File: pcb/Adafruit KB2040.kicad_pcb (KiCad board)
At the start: 2 copper layers, 107.2 x 23.5 mm, 12 parts, among them M1 Vibrating-Motor, SW1 SW_SPST, U1 kb2040, U2 2465

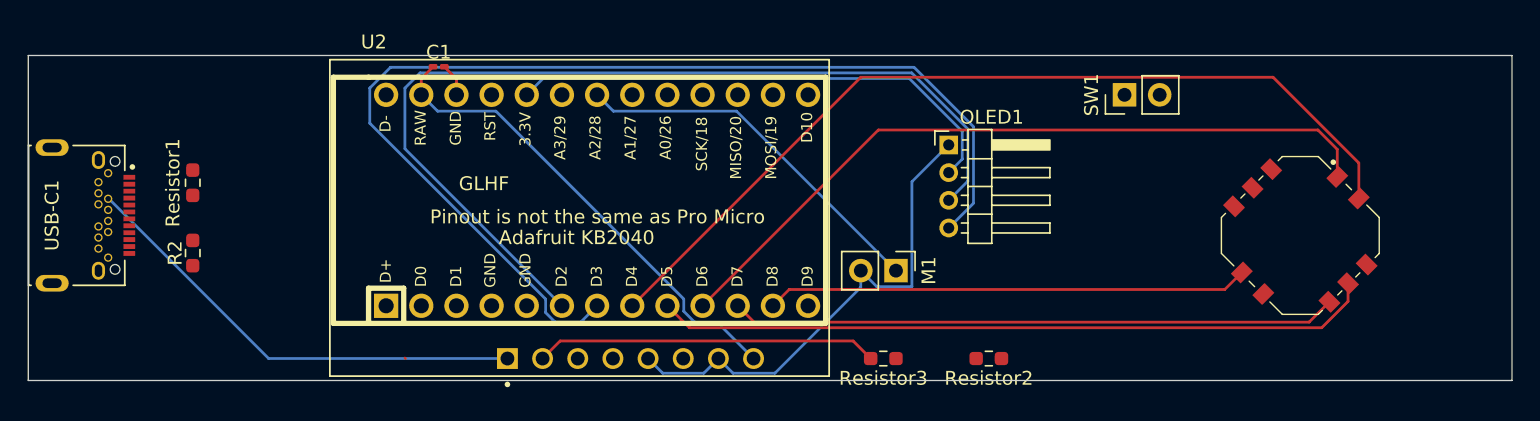
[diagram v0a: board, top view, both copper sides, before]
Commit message: gotta redo the board brahhh - the oled cant fit in the current orientation.
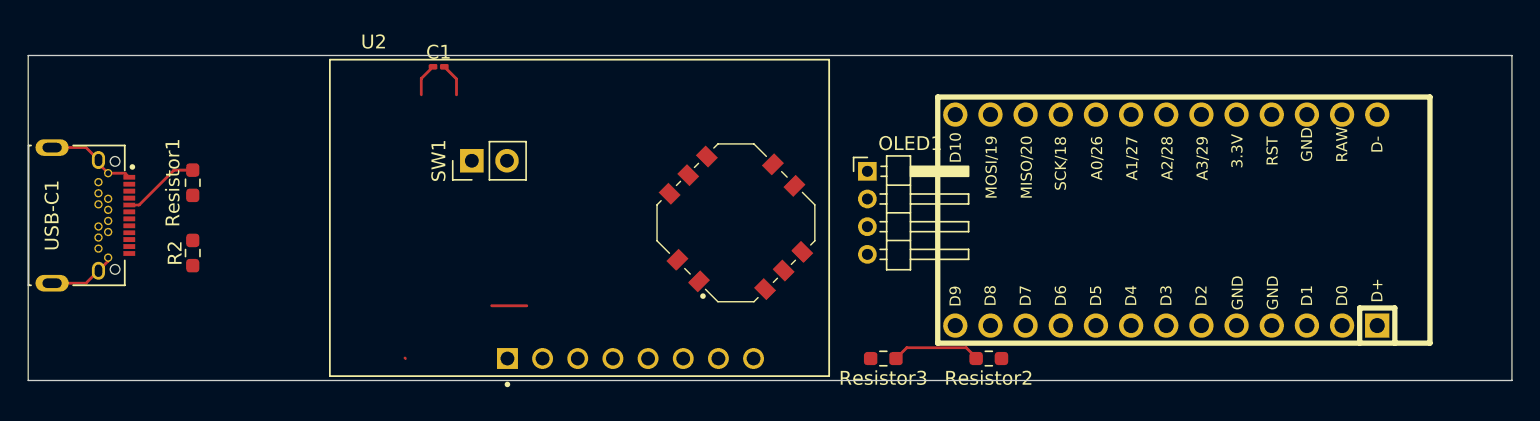
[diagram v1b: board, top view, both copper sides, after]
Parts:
- removed M1: Vibrating-Motor, Connector_PinHeader_2.54mm:PinHeader_1x02_P2.54mm_Vertical
- U1: moved to B.Cu
- moved SW1 47.4 mm to (116.7, 61.9)
- moved U1 43.7 mm to (168.1, 66.2)
- moved D-Pad1 40.8 mm to (135.8, 66.4), turned to 180 degrees
- moved OLED1 6.17 mm to (145.3, 62.7)
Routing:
- net SDA: track 80.0 -> 0.00 mm
- net SDL: track 68.9 -> 0.00 mm
- net D8ASSY: track 64.5 -> 0.00 mm
- net D10ASSY: track 53.7 -> 0.00 mm
- net Net-(U1-D5): track 51.9 -> 0.00 mm
- net Net-(U1-D7): track 43.8 -> 0.00 mm
- net +3.3V: track 36.9 -> 0.00 mm
- net Net-(U1-D8): track 34.9 -> 0.00 mm
- net VBUS: track 33.6 -> 0.00 mm
- net +5V: track 34.8 -> 2.43 mm
- net Net-(M1-+): track 26.9 -> 0.00 mm
- net Net-(U2-VLIPO): track 24.8 -> 0.00 mm
- net GND: track 38.3 -> 16.5 mm
- net Net-(U1-A0/26): track 0.00 -> 6.48 mm
- net Net-(USB-C1-CC1): track 0.00 -> 5.63 mm

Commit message: I messed around with the wiring more - now it should be done. need to do some final checks before sent off (whatever that means)
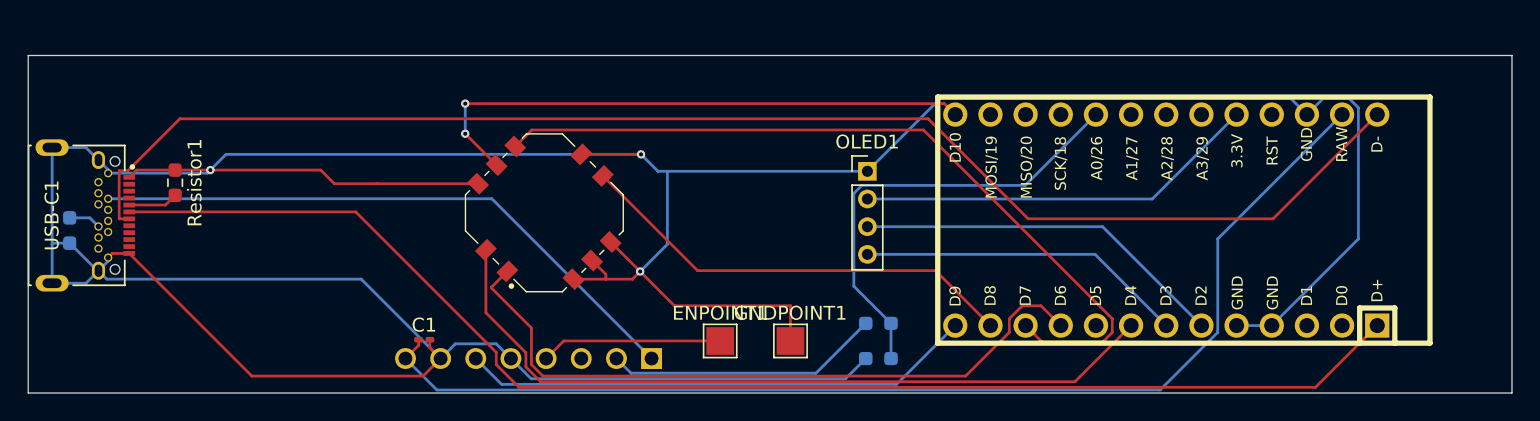
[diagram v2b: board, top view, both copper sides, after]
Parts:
- removed SW1: SW_SPST, Connector_PinHeader_2.54mm:PinHeader_1x02_P2.54mm_Vertical
- added ENPOINT1: TestPoint_Small, TestPoint:TestPoint_Pad_2.0x2.0mm, F.Cu at (134.6, 74.9)
- added GNDPOINT1: TestPoint_Small, TestPoint:TestPoint_Pad_2.0x2.0mm, F.Cu at (139.7, 74.9)
- OLED1: footprint Connector_PinHeader_2.00mm:PinHeader_1x04_P2.00mm_Horizontal -> Connector_PinHeader_2.00mm:PinHeader_1x04_P2.00mm_Vertical
- R2, Resistor2, Resistor3, U2: moved to B.Cu
- moved C1 19.7 mm to (113.2, 74.8)
- moved D-Pad1 13.9 mm to (121.9, 65.7)
- moved R2 9.04 mm to (87.6, 67.0), turned to 90 degrees
- moved Resistor2 7.98 mm to (146.1, 76.2), turned to 0 degrees
- moved Resistor3 2.57 mm to (146.1, 73.7)
- moved Resistor1 1.27 mm to (95.2, 63.5), turned to -90 degrees
- turned U2 to 180 degrees
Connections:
- D-Pad1 pad 1: D10ASSY -> D6ASSY
- D-Pad1 pad 4: Net-(U1-D5) -> D10ASSY
- U1 pad 10: D10ASSY -> D6ASSY
- U1 pad 20: Net-(M1-+) -> unconnected-(U1-A2/28-Pad20)
- U1 pad 26: unconnected-(U1-D10-Pad26) -> D10ASSY
- U1 pad 9: Net-(U1-D5) -> unconnected-(U1-D5-Pad9)
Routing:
- net GND: track 16.5 -> 292.2 mm, vias 0 -> 3
- net D-: track 0.00 -> 102.7 mm
- net D+: track 0.00 -> 97.8 mm
- net +5V: track 2.43 -> 82.5 mm
- net Net-(U1-D7): track 0.00 -> 57.3 mm
- net D8ASSY: track 0.00 -> 55.5 mm
- net D6ASSY: track 0.00 -> 50.3 mm
- net VBUS: track 0.00 -> 44.0 mm
- net D10ASSY: track 0.00 -> 41.1 mm, vias 0 -> 2
- net LBO: track 0.00 -> 37.2 mm
- net Net-(U1-D8): track 0.00 -> 32.5 mm
- net +3.3V: track 0.00 -> 29.2 mm
- net SDL: track 0.00 -> 27.1 mm
- net Net-(U1-A0/26): track 6.48 -> 32.9 mm
- net SDA: track 0.00 -> 23.7 mm
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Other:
- board size 107.2 x 23.5 mm -> 107.2 x 24.4 mm

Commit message: Maybe finished the board? looks good to me. gonna look it over with others first
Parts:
- added C2: 0.1uF, Capacitor_SMD:C_0201_0603Metric_Pad0.64x0.40mm_HandSolder, F.Cu at (142.2, 63.5)
- added C3: 0.1uF, Capacitor_SMD:C_0201_0603Metric_Pad0.64x0.40mm_HandSolder, F.Cu at (174.2, 56.5)
- added C4: 0.1uF, Capacitor_SMD:C_0201_0603Metric_Pad0.64x0.40mm_HandSolder, F.Cu at (178.4, 56.5)
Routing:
- net GND: track 292.2 -> 301.2 mm
- net +3.3V: track 29.2 -> 35.4 mm
- net +5V: track 82.5 -> 84.9 mm
- added copper zone on B.Cu, net GND
- added copper zone on F.Cu, net GND

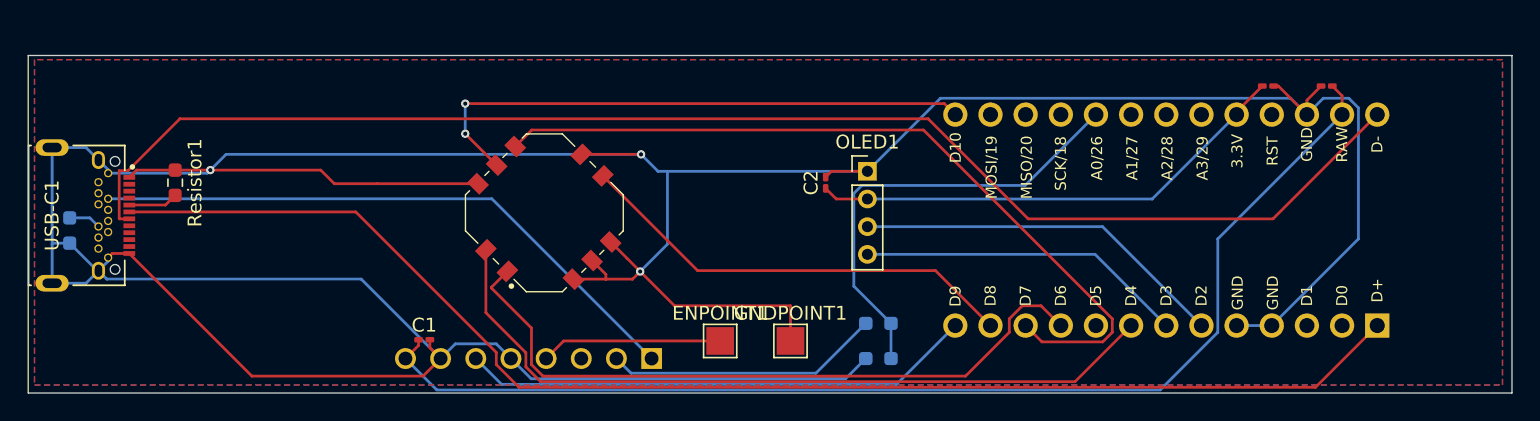
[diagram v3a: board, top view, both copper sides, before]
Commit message: Refreshed th eoled design to accomodate the screen i found - swapped vcc and gnd
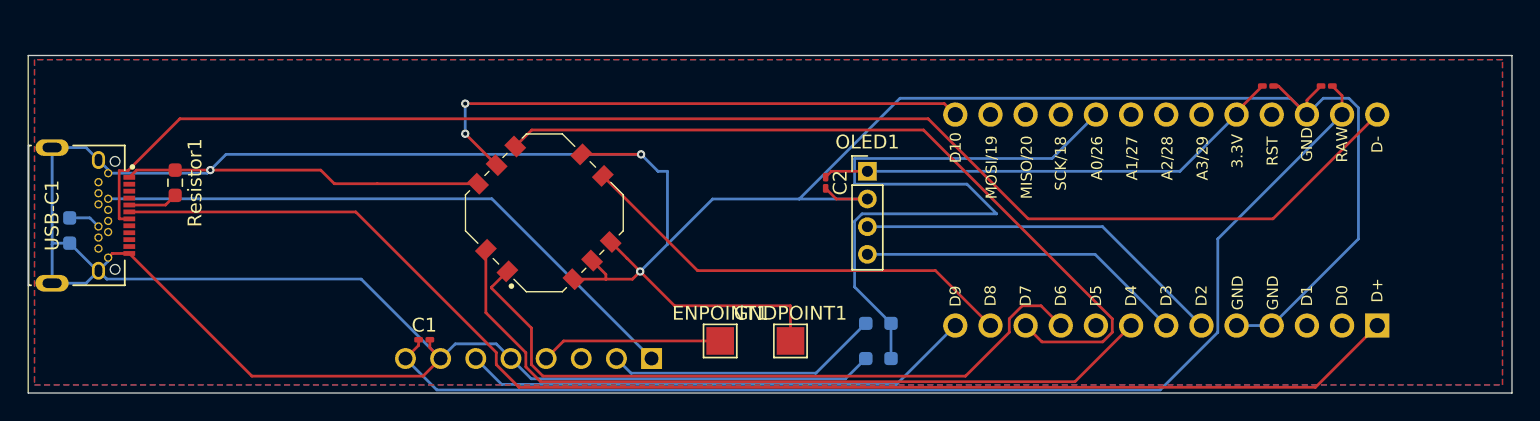
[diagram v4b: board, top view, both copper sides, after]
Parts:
- turned C2 to -90 degrees
- turned C3 to 0 degrees
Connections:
- C3 pad 1: GND -> +3.3V
- C3 pad 2: +3.3V -> GND
- OLED1 pad 1: GND -> +3.3V
- OLED1 pad 2: +3.3V -> GND
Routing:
- net Net-(U1-A0/26): track 32.9 -> 53.2 mm
- net GND: track 301.2 -> 308.4 mm
- net +3.3V: track 35.4 -> 34.4 mm
